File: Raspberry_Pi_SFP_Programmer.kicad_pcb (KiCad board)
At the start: 2 copper layers, 65 x 56 mm, 18 parts, among them J1 RPi_GPIO, J2 SFP+, J4 Conn_02x03_Odd_Even, Q1 BC847, Q2 BC847

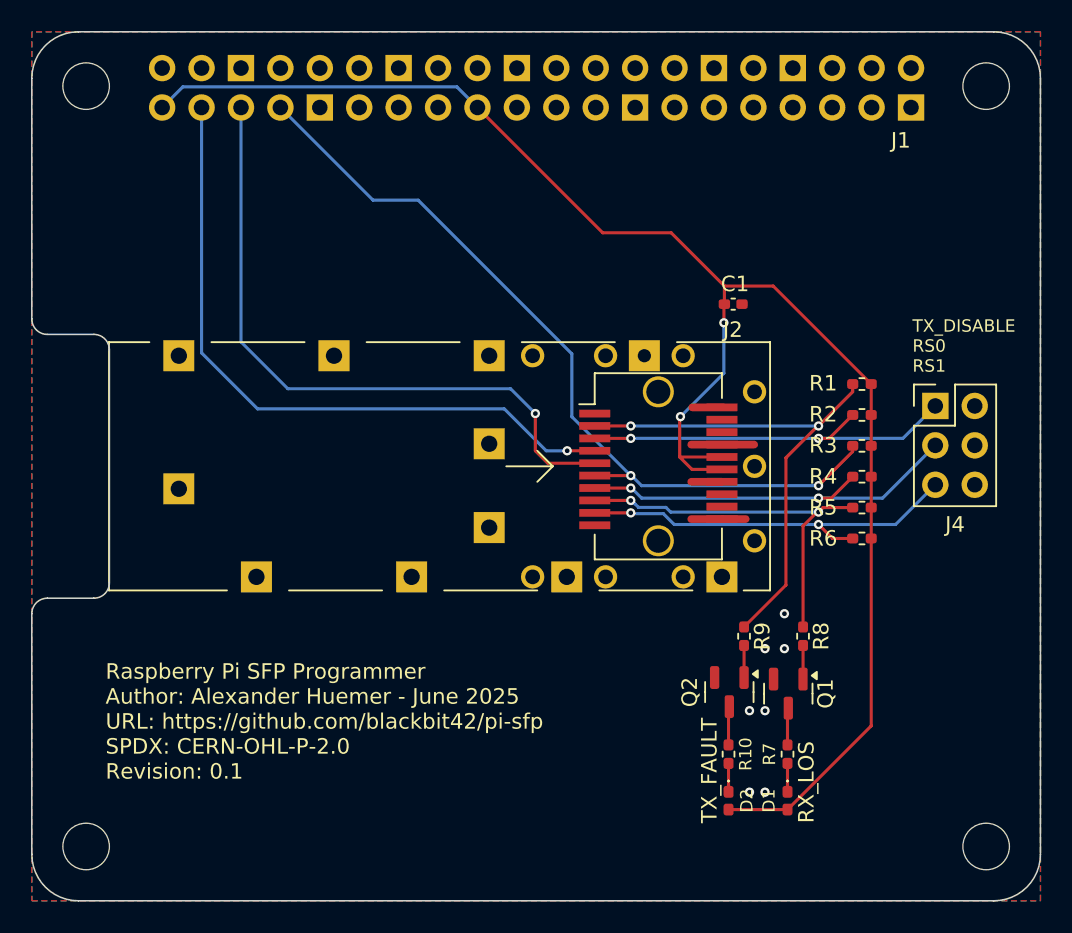
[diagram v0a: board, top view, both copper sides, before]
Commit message: Multiple improvements
Fix 3.3V rail decoupling
Derive VccT and VccR from 5V
Add power supply filter networks
Replace jumper pin header with dip switch
Add LED for MOD_ABS
Connect RX_LOS and TX_FAULT to GPIOs
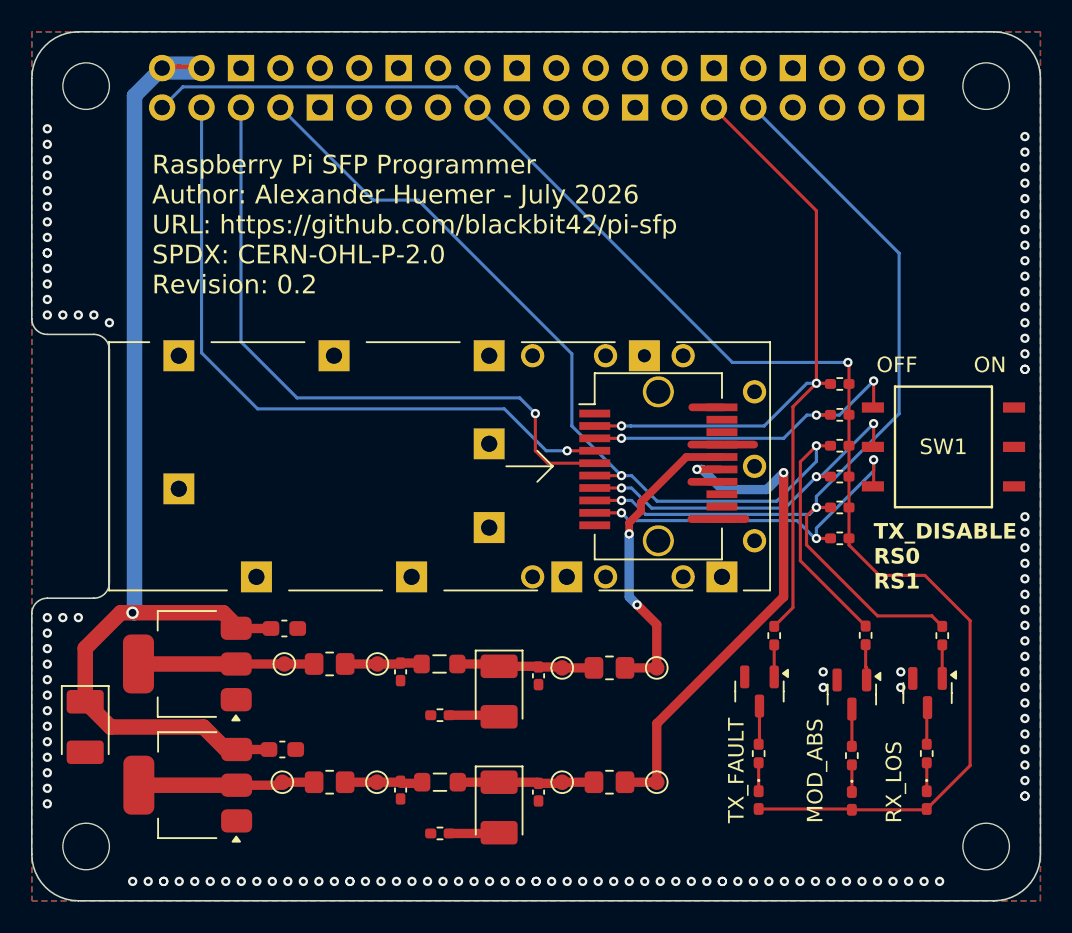
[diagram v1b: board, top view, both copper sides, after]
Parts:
- removed C1: 1u, Capacitor_SMD:C_0402_1005Metric_Pad0.74x0.62mm_HandSolder
- removed J4: Conn_02x03_Odd_Even, Connector_PinHeader_2.54mm:PinHeader_2x03_P2.54mm_Vertical
- added C12: 1u, Capacitor_SMD:C_0603_1608Metric_Pad1.08x0.95mm_HandSolder, F.Cu at (72.8, 92.2)
- added C13: 1u, Capacitor_SMD:C_0603_1608Metric_Pad1.08x0.95mm_HandSolder, F.Cu at (72.6, 100.0)
- added C14: 22u, Capacitor_Tantalum_SMD:CP_EIA-3528-21_Kemet-B_HandSolder, F.Cu at (59.9, 98.6)
- added C2: 0.1u, Capacitor_SMD:C_0402_1005Metric_Pad0.74x0.62mm_HandSolder, F.Cu at (80.3, 95.0)
- added C3: 22u, Capacitor_Tantalum_SMD:CP_EIA-3528-21_Kemet-B_HandSolder, F.Cu at (86.6, 96.3)
- added C4: 0.1u, Capacitor_SMD:C_0402_1005Metric_Pad0.74x0.62mm_HandSolder, F.Cu at (89.2, 95.2)
- added C5: 0.1u, Capacitor_SMD:C_0402_1005Metric_Pad0.74x0.62mm_HandSolder, F.Cu at (80.3, 102.6)
- added C6: 22u, Capacitor_Tantalum_SMD:CP_EIA-3528-21_Kemet-B_HandSolder, F.Cu at (86.6, 103.7)
- added C7: 0.1u, Capacitor_SMD:C_0402_1005Metric_Pad0.74x0.62mm_HandSolder, F.Cu at (89.2, 102.8)
- added D3: LED, LED_SMD:LED_0402_1005Metric_Pad0.77x0.64mm_HandSolder, F.Cu at (109.3, 103.3)
- added L1: 4.7u, Inductor_SMD:L_0805_2012Metric_Pad1.05x1.20mm_HandSolder, F.Cu at (82.8, 94.5)
- added L2: 4.7u, Inductor_SMD:L_0805_2012Metric_Pad1.05x1.20mm_HandSolder, F.Cu at (82.8, 102.1)
- added Q3: BC847, Package_TO_SOT_SMD:SOT-23, F.Cu at (109.3, 96.5)
- added R11: 0.1, Resistor_SMD:R_0805_2012Metric_Pad1.20x1.40mm_HandSolder, F.Cu at (75.7, 94.5)
- added R12: 0.5, Resistor_SMD:R_0402_1005Metric_Pad0.72x0.64mm_HandSolder, F.Cu at (82.8, 97.8)
- added R13: 0.5, Resistor_SMD:R_0402_1005Metric_Pad0.72x0.64mm_HandSolder, F.Cu at (82.8, 105.4)
- added R14: 0.1, Resistor_SMD:R_0805_2012Metric_Pad1.20x1.40mm_HandSolder, F.Cu at (75.7, 102.1)
- added R15: 10k, Resistor_SMD:R_0402_1005Metric_Pad0.72x0.64mm_HandSolder, F.Cu at (110.2, 92.6)
- added R16: 5k, Resistor_SMD:R_0402_1005Metric_Pad0.72x0.64mm_HandSolder, F.Cu at (109.3, 100.4)
- added R17: 0.1, Resistor_SMD:R_0805_2012Metric_Pad1.20x1.40mm_HandSolder, F.Cu at (93.7, 94.7)
- added R18: 0.1, Resistor_SMD:R_0805_2012Metric_Pad1.20x1.40mm_HandSolder, F.Cu at (93.7, 102.1)
- added SW1: EDS03SGNNTR04Q, Raspberry_Pi_SFP_Programmer:SW_2319847_TEC, F.Cu at (115.2, 80.5)
- added TP1: TestPoint, TestPoint:TestPoint_Pad_D1.0mm, F.Cu at (72.8, 94.5)
- added TP2: TestPoint, TestPoint:TestPoint_Pad_D1.0mm, F.Cu at (78.8, 94.5)
- added TP3: TestPoint, TestPoint:TestPoint_Pad_D1.0mm, F.Cu at (72.6, 102.1)
- added TP4: TestPoint, TestPoint:TestPoint_Pad_D1.0mm, F.Cu at (78.7, 102.1)
- added TP5: TestPoint, TestPoint:TestPoint_Pad_D1.0mm, F.Cu at (90.7, 94.7)
- added TP6: TestPoint, TestPoint:TestPoint_Pad_D1.0mm, F.Cu at (96.8, 94.7)
- added TP7: TestPoint, TestPoint:TestPoint_Pad_D1.0mm, F.Cu at (90.7, 102.1)
- added TP8: TestPoint, TestPoint:TestPoint_Pad_D1.0mm, F.Cu at (96.8, 102.1)
- added U1: AMS1117-3.3, Package_TO_SOT_SMD:SOT-223-3_TabPin2, F.Cu at (66.5, 94.5)
- added U2: AMS1117-3.3, Package_TO_SOT_SMD:SOT-223-3_TabPin2, F.Cu at (66.5, 102.3)
- R10, R7: value 330 -> 5k
- moved D1 8.97 mm to (114.2, 103.3)
- moved Q1 8.97 mm to (114.2, 96.4)
- moved R7 8.97 mm to (114.2, 100.3)
- moved R8 8.97 mm to (115.2, 92.7)
- moved D2 1.94 mm to (103.3, 103.3)
- moved Q2 1.94 mm to (103.4, 96.3)
- moved R10 1.94 mm to (103.3, 100.3)
- moved R9 1.94 mm to (104.3, 92.7)
- moved R3 1.43 mm to (108.6, 80.4)
- moved R6 1.43 mm to (108.6, 86.4)
- moved R1 1.43 mm to (108.6, 76.4)
- moved R2 1.43 mm to (108.6, 78.4)
- moved R4 1.43 mm to (108.6, 82.4)
- moved R5 1.43 mm to (108.6, 84.4)
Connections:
- J1 pad 2: unconnected-(J1-5V-Pad2) -> +5V
- J1 pad 29: unconnected-(J1-BCM5-Pad29) -> /TX_FAULT
- J1 pad 31: unconnected-(J1-BCM6-Pad31) -> /RX_LOS
- J1 pad 4: unconnected-(J1-5V-Pad4) -> +5V
- J2 pad 15: +3.3V -> VccR
- J2 pad 16: +3.3V -> VccT
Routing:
- net +5V: track 0.00 -> 70.5 mm, vias 0 -> 1
- net /RX_LOS: track 25.0 -> 61.6 mm
- net VccR: track 0.00 -> 33.5 mm, vias 0 -> 2
- net /TX_FAULT: track 33.0 -> 53.6 mm
- net VccT: track 0.00 -> 20.2 mm, vias 0 -> 2
- net /MOD_ABS: track 53.0 -> 66.3 mm
- net Net-(U1-VO): track 0.00 -> 11.3 mm
- net Net-(U2-VO): track 0.00 -> 11.1 mm
- net Net-(C6-Pad1): track 0.00 -> 8.62 mm
- net Net-(C3-Pad1): track 0.00 -> 8.55 mm
- net +3.3V: track 105.6 -> 97.7 mm, vias 2 -> 1
- net Net-(C2-Pad1): track 0.00 -> 5.28 mm
- net Net-(C5-Pad1): track 0.00 -> 4.81 mm
- net /TX_DISABLE: track 25.6 -> 22.2 mm, vias 2 -> 3
- net Net-(C6-Pad2): track 0.00 -> 3.17 mm
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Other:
- board text added: "MOD_ABS"
- board text added: "Raspberry Pi SFP Programmer Author: Alexander Huemer - July 2026 URL: https://github.com/blackbit42/pi-sfp SPDX: CERN-OHL-P-2.0 Revision: 0.2"
- board text removed: "Raspberry Pi SFP Programmer Author: Alexander Huemer - June 2025 URL: https://github.com/blackbit42/pi-sfp SPDX: CERN-OHL-P-2.0 Revision: 0.1"
